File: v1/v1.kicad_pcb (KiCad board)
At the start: 2 copper layers, 48.3 x 30.5 mm, 10 parts, among them J3 PWR, J4 RGB, U1 WeMos_D1_mini, U2 LevelShifter

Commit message: angled capacitor
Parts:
- C_PWR1: footprint Capacitor_THT:CP_Radial_D10.0mm_P5.00mm -> w_capacitors:CP_10x16mm_hor
- moved C_PWR1 9.63 mm to (105.8, 68.6), turned to 0 degrees

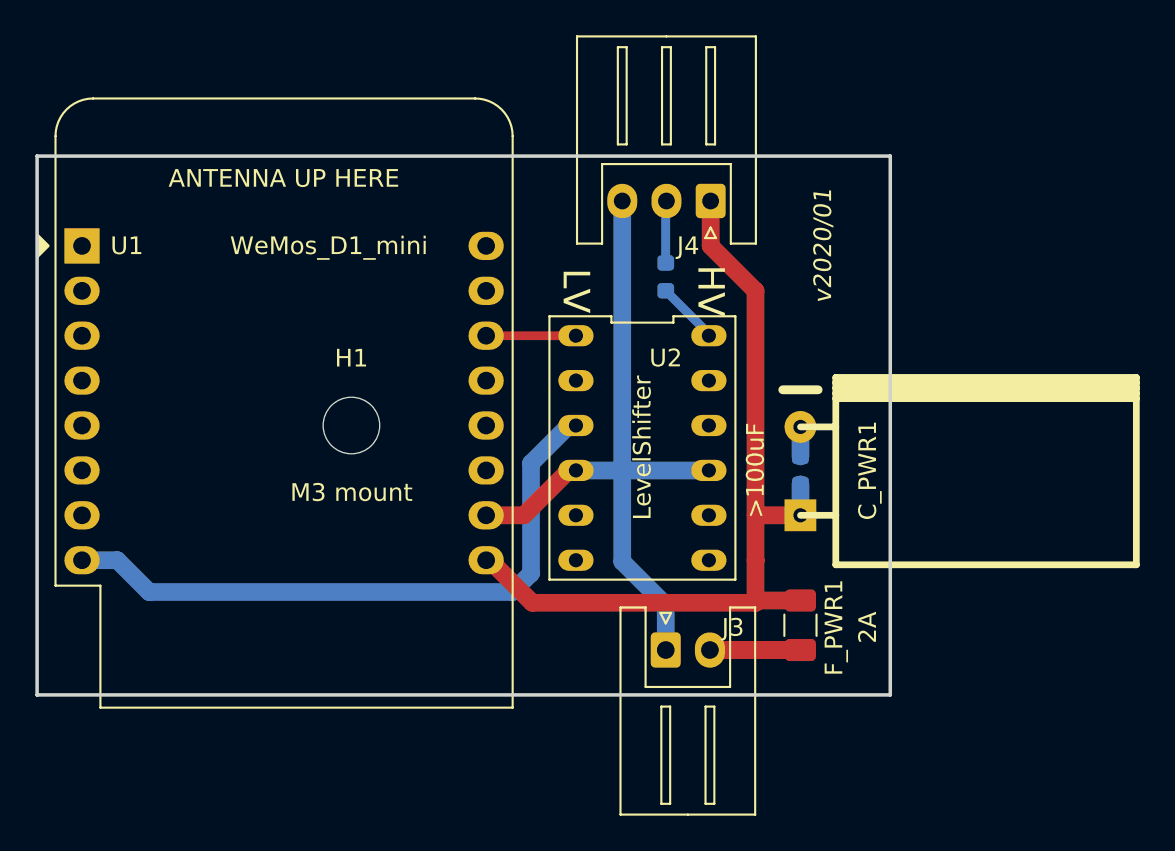
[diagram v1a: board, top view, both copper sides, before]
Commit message: refine version number and add logo to top
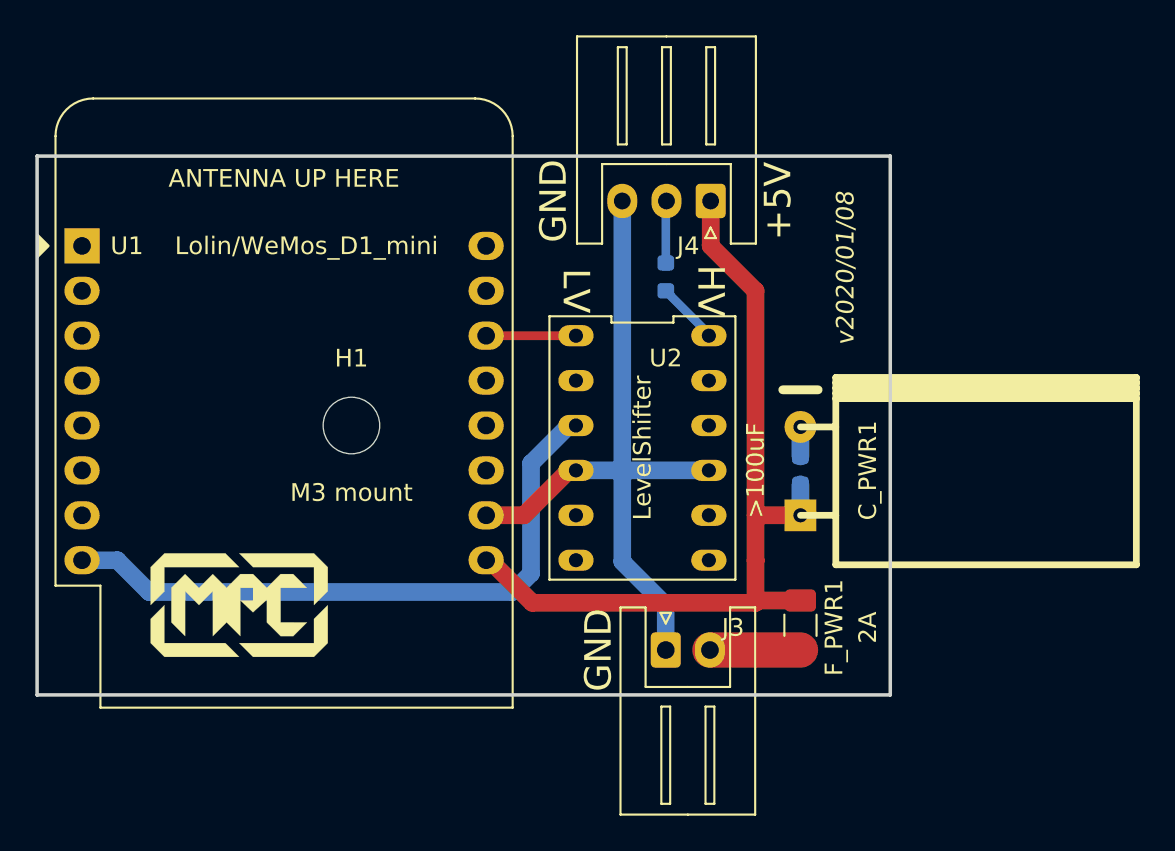
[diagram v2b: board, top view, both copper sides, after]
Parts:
- added G***: LOGO, libs:mpc_logo_10mm, F.Cu at (64.8, 76.2)
- U1: value WeMos_D1_mini -> Lolin/WeMos_D1_mini
- moved G*** 4.58 mm to (67.3, 73.7)
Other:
- board text added: "+5V"
- board text added: "GND"
- board text added: "v2020/01/08"
- board text removed: "v2020/01"
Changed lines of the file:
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@@
-(kicad_pcb (version 20171130) (host pcbnew "(5.1.0)-1")
+(kicad_pcb (version 20171130) (host pcbnew "(5.1.2)-1")
   (general
     (thickness 1.6)
-    (drawings 11)
+    (drawings 14)
     (tracks 43)
     (zones 0)
-    (modules 10)
+    (modules 11)
     (nets 8)
   )
@@
     (add_net GND)
   )
+  (module libs:mpc_logo_10mm (layer F.Cu)
+    (at 64.77 76.2)
+    (fp_text reference G*** (at 0 0) (layer F.SilkS) hide
+      (effects (font (size 1.524 1.524) (thickness 0.3)))
+    )
+    (fp_text value LOGO (at 0.75 0) (layer F.SilkS) hide
+      (effects (font (size 1.524 1.524) (thickness 0.3)))
+    )
+    (fp_poly (pts (xy 4.62029 -2.538012) (xy 5.011208 -2.147087) (xy 5.011208 -0.781837) (xy 4.620948 -0.391583)
+      (xy 4.230688 -0.00133) (xy 4.230688 -2.148417) (xy 0.781837 -2.148417) (xy 0.391583 -2.538677)
+      (xy 0.00133 -2.928937) (xy 4.229371 -2.928937) (xy 4.62029 -2.538012)) (layer F.SilkS) (width 0.01))
+    (fp_poly (pts (xy -0.388937 -2.538677) (xy 0.001316 -2.148417) (xy -4.228042 -2.148417) (xy -4.228042 -0.778965)
+      (xy -4.613672 -0.394035) (xy -4.651454 -0.356327) (xy -4.68827 -0.319593) (xy -4.723942 -0.284011)
+      (xy -4.758292 -0.249756) (xy -4.791143 -0.217006) (xy -4.822318 -0.185938) (xy -4.85164 -0.156727)
+      (xy -4.87893 -0.12955) (xy -4.904012 -0.104585) (xy -4.926708 -0.082007) (xy -4.94684 -0.061994)
+      (xy -4.964231 -0.044722) (xy -4.978704 -0.030367) (xy -4.990082 -0.019106) (xy -4.998186 -0.011116)
+      (xy -5.00284 -0.006574) (xy -5.003932 -0.005552) (xy -5.00432 -0.00542) (xy -5.004685 -0.005737)
+      (xy -5.005029 -0.006654) (xy -5.005352 -0.008321) (xy -5.005654 -0.010889) (xy -5.005937 -0.014509)
+      (xy -5.006202 -0.01933) (xy -5.006447 -0.025504) (xy -5.006676 -0.03318) (xy -5.006887 -0.042511)
+      (xy -5.007082 -0.053646) (xy -5.007261 -0.066735) (xy -5.007425 -0.08193) (xy -5.007575 -0.099381)
+      (xy -5.007712 -0.119239) (xy -5.007835 -0.141654) (xy -5.007945 -0.166777) (xy -5.008044 -0.194758)
+      (xy -5.008132 -0.225747) (xy -5.00821 -0.259897) (xy -5.008277 -0.297356) (xy -5.008336 -0.338276)
+      (xy -5.008386 -0.382808) (xy -5.008428 -0.431101) (xy -5.008463 -0.483306) (xy -5.008492 -0.539575)
+      (xy -5.008514 -0.600057) (xy -5.008531 -0.664903) (xy -5.008544 -0.734264) (xy -5.008553 -0.80829)
+      (xy -5.008559 -0.887132) (xy -5.008562 -0.970941) (xy -5.008562 -2.1471) (xy -4.617637 -2.538019)
+      (xy -4.226712 -2.928937) (xy -0.779191 -2.928937) (xy -0.388937 -2.538677)) (layer F.SilkS) (width 0.01))
+    (fp_poly (pts (xy -2.754167 -1.453586) (xy -2.718955 -1.418579) (xy -2.683767 -1.383597) (xy -2.648882 -1.348916)
+      (xy -2.61458 -1.314816) (xy -2.58114 -1.281574) (xy -2.548842 -1.249467) (xy -2.517965 -1.218773)
+      (xy -2.488788 -1.18977) (xy -2.46159 -1.162735) (xy -2.436652 -1.137947) (xy -2.414252 -1.115683)
+      (xy -2.39467 -1.096221) (xy -2.378185 -1.079838) (xy -2.365077 -1.066812) (xy -2.361379 -1.063138)
+      (xy -2.274038 -0.976361) (xy -1.49358 -1.756833) (xy -0.71216 -0.975427) (xy -0.416348 -1.272865)
+      (xy -0.381627 -1.307778) (xy -0.346832 -1.342767) (xy -0.312254 -1.377541) (xy -0.278183 -1.411808)
+      (xy -0.244909 -1.445275) (xy -0.212722 -1.47765) (xy -0.181913 -1.508642) (xy -0.152772 -1.537959)
+      (xy -0.125588 -1.565308) (xy -0.100653 -1.590398) (xy -0.078257 -1.612937) (xy -0.058689 -1.632632)
+      (xy -0.04224 -1.649193) (xy -0.0292 -1.662326) (xy -0.027967 -1.663568) (xy 0.064601 -1.756833)
+      (xy 0.784883 -1.756833) (xy 1.174489 -1.36661) (xy 1.564094 -0.976387) (xy 1.863467 -1.277314)
+      (xy 1.898295 -1.312324) (xy 1.933134 -1.347348) (xy 1.967701 -1.382102) (xy 2.001713 -1.416302)
+      (xy 2.034888 -1.449661) (xy 2.066941 -1.481896) (xy 2.09759 -1.512722) (xy 2.126552 -1.541853)
+      (xy 2.153543 -1.569006) (xy 2.178281 -1.593896) (xy 2.200482 -1.616237) (xy 2.219864 -1.635745)
+      (xy 2.236142 -1.652135) (xy 2.249035 -1.665123) (xy 2.25143 -1.667536) (xy 2.340019 -1.756833)
+      (xy 3.057267 -1.756833) (xy 3.837775 -0.976313) (xy 3.090991 -0.976313) (xy 2.344208 -0.976312)
+      (xy 2.344208 0.976313) (xy 3.092318 0.976432) (xy 3.840427 0.976552) (xy 3.449295 1.366693)
+      (xy 3.058164 1.756833) (xy 2.701848 1.756696) (xy 2.345531 1.756558) (xy 1.954556 1.367097)
+      (xy 1.56358 0.977635) (xy 1.562972 0.338453) (xy 1.562365 -0.300728) (xy 1.172104 0.054562)
+      (xy 1.133313 0.089867) (xy 1.095561 0.124205) (xy 1.059033 0.157409) (xy 1.023918 0.18931)
+      (xy 0.9904 0.219738) (xy 0.958666 0.248525) (xy 0.928903 0.275504) (xy 0.901297 0.300503)
+      (xy 0.876034 0.323357) (xy 0.853301 0.343894) (xy 0.833285 0.361947) (xy 0.816172 0.377348)
+      (xy 0.802147 0.389927) (xy 0.791398 0.399515) (xy 0.784112 0.405945) (xy 0.780473 0.409046)
+      (xy 0.78008 0.409317) (xy 0.778008 0.40747) (xy 0.772288 0.40216) (xy 0.763111 0.393568)
+      (xy 0.750668 0.381874) (xy 0.73515 0.367259) (xy 0.716747 0.349902) (xy 0.69565 0.329984)
+      (xy 0.67205 0.307685) (xy 0.646138 0.283186) (xy 0.618104 0.256666) (xy 0.588139 0.228306)
+      (xy 0.556433 0.198287) (xy 0.523178 0.166788) (xy 0.488564 0.13399) (xy 0.452782 0.100072)
+      (xy 0.425373 0.074083) (xy 0.07243 -0.260615) (xy 0.426475 -0.261286) (xy 0.780521 -0.261957)
+      (xy 0.780521 -0.976312) (xy 0.068754 -0.976312) (xy 0.068792 -0.619786) (xy 0.068795 -0.590184)
+      (xy 0.068797 -0.555567) (xy 0.0688 -0.516213) (xy 0.068802 -0.4724) (xy 0.068804 -0.424405)
+      (xy 0.068806 -0.372506) (xy 0.068808 -0.316979) (xy 0.068809 -0.258103) (xy 0.068811 -0.196154)
+      (xy 0.068812 -0.131411) (xy 0.068813 -0.064151) (xy 0.068814 0.00535) (xy 0.068814 0.076813)
+      (xy 0.068815 0.149962) (xy 0.068815 0.376743) (xy 0.068814 0.453857) (xy 0.068813 0.531269)
+      (xy 0.068813 0.608702) (xy 0.068811 0.685878) (xy 0.06881 0.746122) (xy 0.068792 1.755504)
+      (xy -0.320976 1.365742) (xy -0.710744 0.975981) (xy -1.090503 1.356485) (xy -1.128049 1.394109)
+      (xy -1.164672 1.430818) (xy -1.200192 1.46643) (xy -1.234426 1.500762) (xy -1.267193 1.533632)
+      (xy -1.298312 1.564858) (xy -1.327601 1.594257) (xy -1.354878 1.621646) (xy -1.379962 1.646844)
+      (xy -1.40267 1.669668) (xy -1.422823 1.689935) (xy -1.440237 1.707464) (xy -1.454732 1.722071)
+      (xy -1.466125 1.733575) (xy -1.474236 1.741793) (xy -1.478882 1.746542) (xy -1.479862 1.747573)
+      (xy -1.489461 1.758156) (xy -1.489533 0.488573) (xy -1.489604 -0.781011) (xy -1.88173 -0.390389)
+      (xy -2.273855 0.000232) (xy -2.664896 -0.390803) (xy -3.055937 -0.781837) (xy -3.055937 1.755504)
+      (xy -3.446198 1.36525) (xy -3.836458 0.974996) (xy -3.836458 -0.976785) (xy -3.573882 -1.240471)
+      (xy -3.540142 -1.274355) (xy -3.505696 -1.30895) (xy -3.470915 -1.343884) (xy -3.436167 -1.378787)
+      (xy -3.401822 -1.413289) (xy -3.368248 -1.447017) (xy -3.335815 -1.479601) (xy -3.304893 -1.510671)
+      (xy -3.275849 -1.539855) (xy -3.249054 -1.566782) (xy -3.224876 -1.591082) (xy -3.203686 -1.612383)
+      (xy -3.185851 -1.630315) (xy -3.185461 -1.630707) (xy -3.059616 -1.757259) (xy -2.754167 -1.453586)) (layer F.SilkS) (width 0.01))
+    (fp_poly (pts (xy 5.011208 2.1471) (xy 4.229358 2.928938) (xy 0.781837 2.928938) (xy 0.391583 2.538677)
+      (xy 0.00133 2.148417) (xy 4.230688 2.148417) (xy 4.230693 1.463807) (xy 4.230698 0.779198)
+      (xy 5.011208 -0.000082) (xy 5.011208 2.1471)) (layer F.SilkS) (width 0.01))
+    (fp_poly (pts (xy -4.228042 2.148417) (xy -0.779191 2.148417) (xy -0.388937 2.538677) (xy 0.001316 2.928938)
+      (xy -4.226725 2.928938) (xy -4.617644 2.538012) (xy -5.008562 2.147087) (xy -5.008562 0.781837)
+      (xy -4.618302 0.391583) (xy -4.228042 0.00133) (xy -4.228042 2.148417)) (layer F.SilkS) (width 0.01))
+  )
   (module w_capacitors:CP_10x16mm_hor (layer F.Cu)
     (at 105.82 68.62)
@@
   )
   (module "MF custom:mpc_logo_10mm" (layer B.Cu)
-    (at 63.5 71.12 180)
+    (at 67.31 73.66 180)
     (fp_text reference G*** (at 0 0 180) (layer B.SilkS) hide
       (effects (font (size 1.524 1.524) (thickness 0.3)) (justify mirror))
@@
       (effects (font (size 1 1) (thickness 0.15)))
     )
-    (fp_text value WeMos_D1_mini (at 13.97 0) (layer F.SilkS)
+    (fp_text value Lolin/WeMos_D1_mini (at 12.7 0) (layer F.SilkS)
       (effects (font (size 1 1) (thickness 0.15)))
     )
@@
     )
   )
-  (gr_text v2020/01 (at 97.79 55.88 90) (layer F.SilkS)
+  (gr_text GND (at 85.09 78.74 90) (layer F.SilkS)
+    (effects (font (size 1.5 1.5) (thickness 0.3)))
+  )
+  (gr_text +5V (at 95.25 53.34 90) (layer F.SilkS)
+    (effects (font (size 1.5 1.5) (thickness 0.3)))
+  )
+  (gr_text GND (at 82.55 53.34 90) (layer F.SilkS)
+    (effects (font (size 1.5 1.5) (thickness 0.3)))
+  )
+  (gr_text v2020/01/08 (at 99.06 57.15 90) (layer F.SilkS)
     (effects (font (size 1 1) (thickness 0.15) italic))
   )
@@
   (segment (start 81.28 68.18) (end 83.42 66.04) (width 1) (layer B.Cu) (net 6))
   (segment (start 91.4 78.74) (end 91.4 78.405058) (width 1) (layer B.Cu) (net 7))
-  (segment (start 96.52 78.74) (end 91.4 78.74) (width 1) (layer F.Cu) (net 7))
+  (segment (start 96.52 78.74) (end 91.4 78.74) (width 2) (layer F.Cu) (net 7))
   (zone (net 0) (net_name "") (layers F&B.Cu) (hatch edge 0.508)
     (connect_pads (clearance 0.508))
